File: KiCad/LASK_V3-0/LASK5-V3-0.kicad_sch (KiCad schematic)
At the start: 56 parts, among them IC1 ICM-42688-P, J1 Conn_01x04, J2 JST_02, J3 Conn_01x04_Pin, J4 USB_C_Receptacle, J5 Conn_01x02, J6 Conn_01x06_Pin, J9 Conn_01x04, Q1 IRLML2060, Q2 VP0610T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

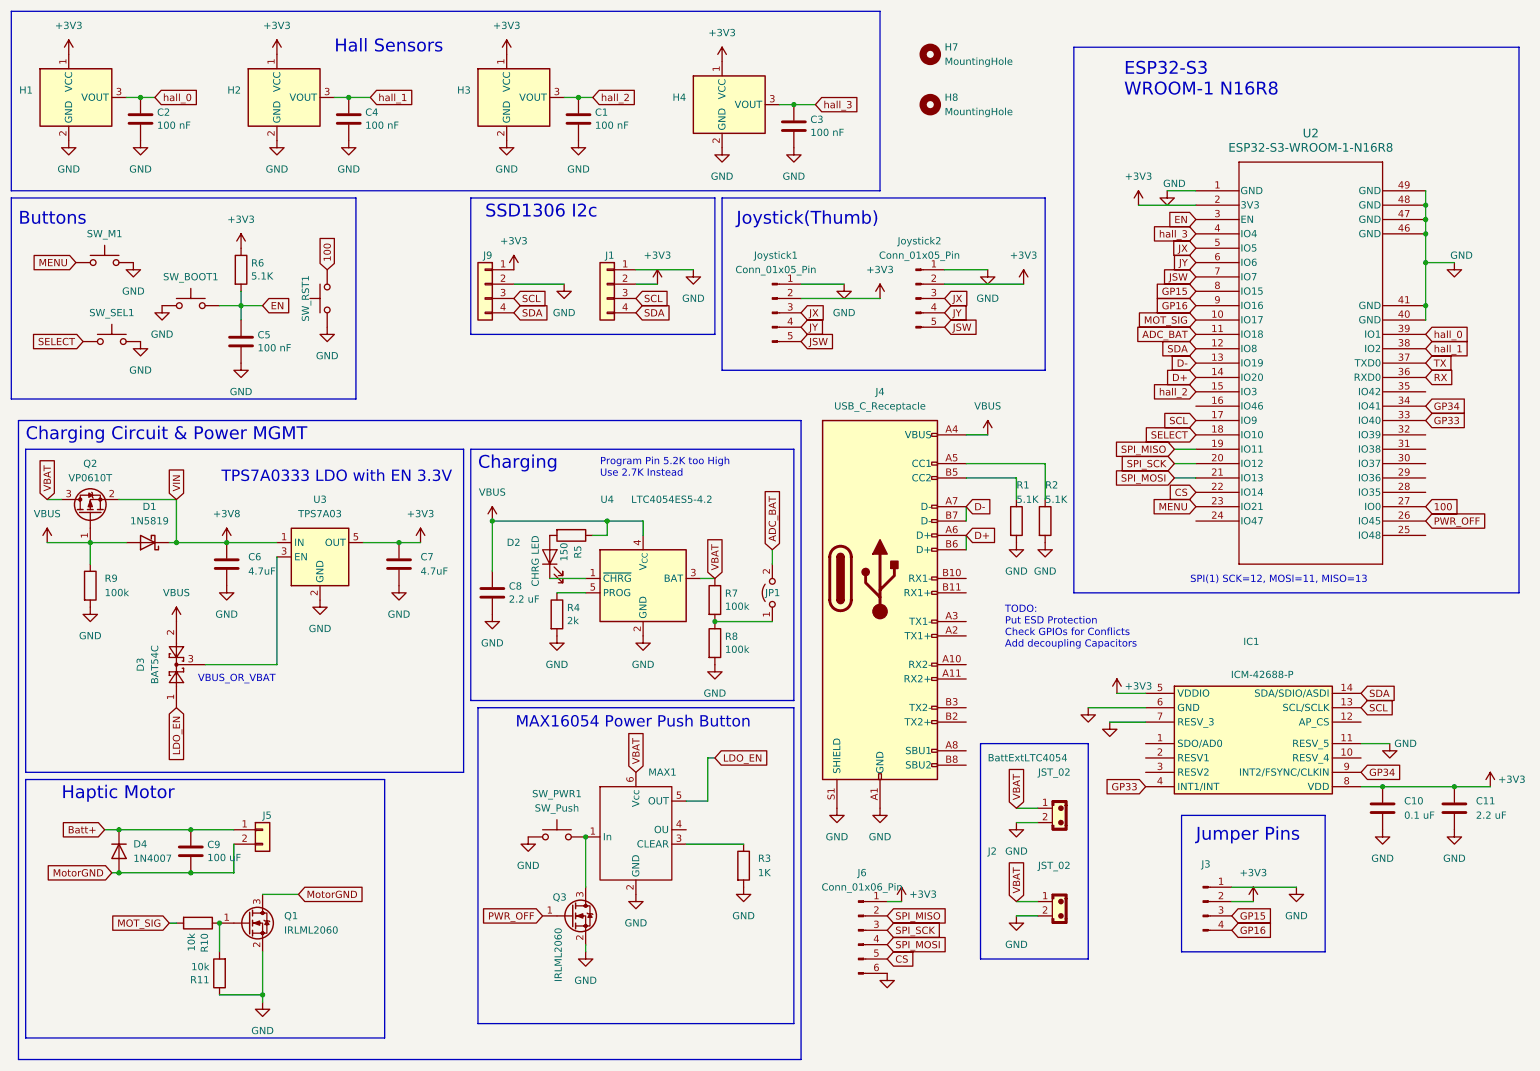
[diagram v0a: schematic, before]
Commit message: Update LASK5 V3 schematic and PCB; add design backups
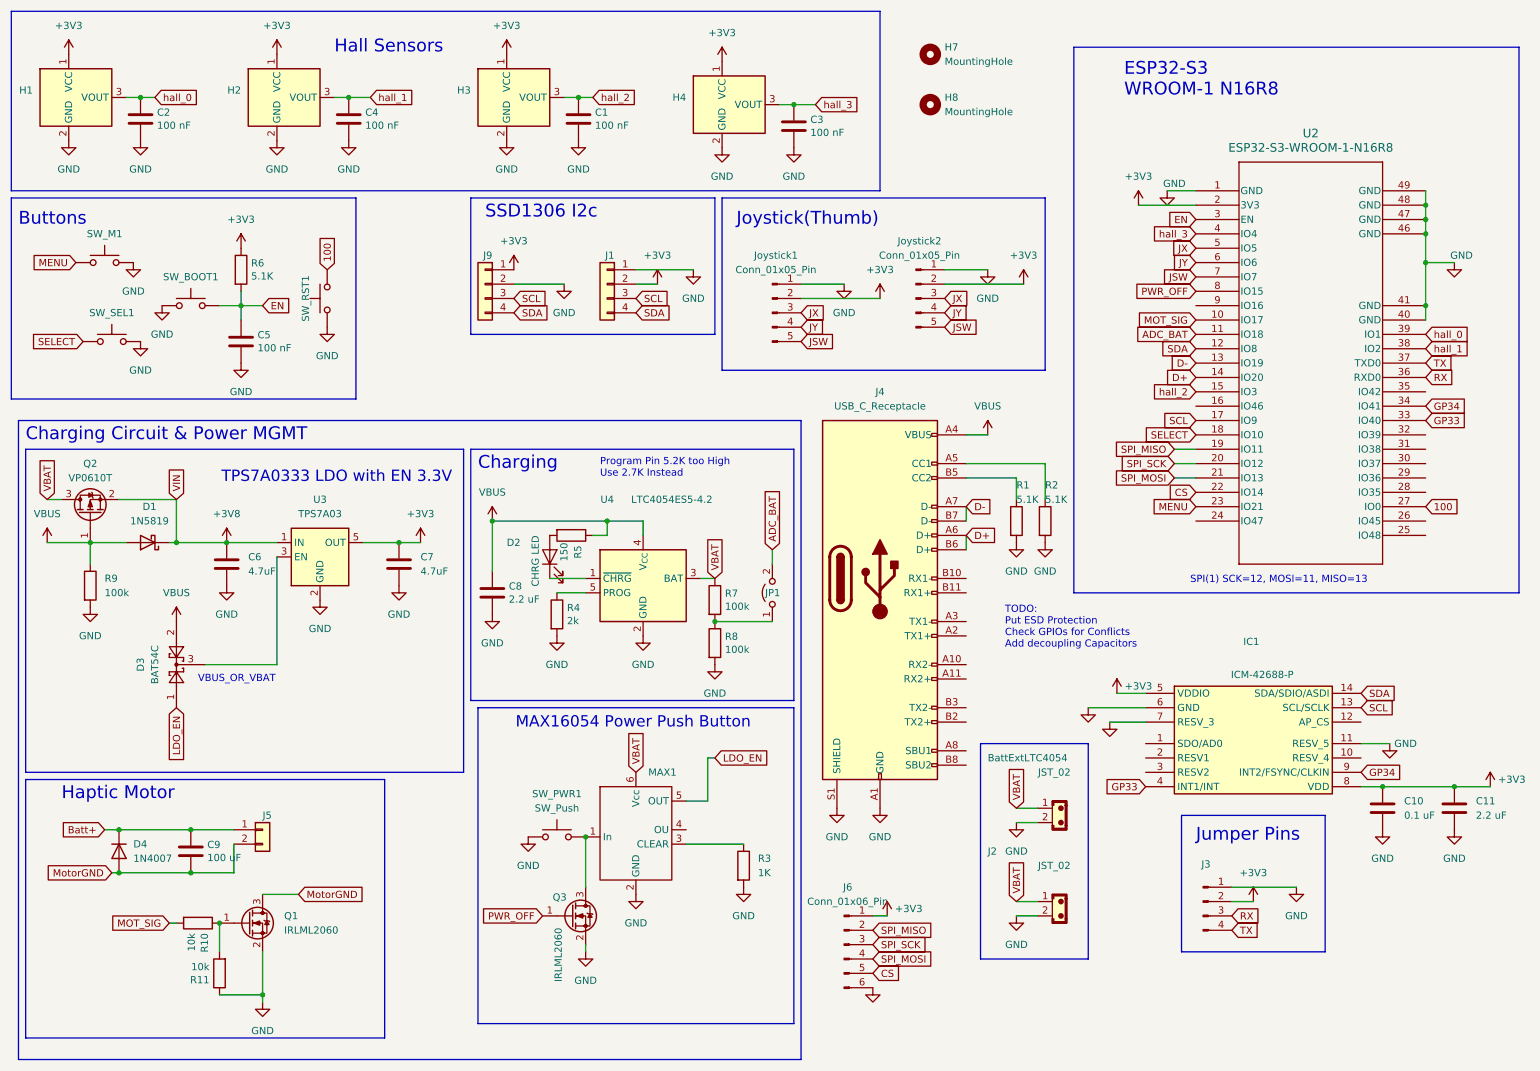
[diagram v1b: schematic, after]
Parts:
- C1, C2, C3, C4, C5: footprint Capacitor_SMD:C_0402_1005Metric -> Capacitor_SMD:C_0603_1608Metric
- MAX1: value ~ -> (none)
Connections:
- net PWR_OFF: now also U2.8 (IO15); no longer U2.26 (IO45)
- net RX: now also J3.3 (Pin_3)
- net TX: now also J3.4 (Pin_4)
- removed net GP15: J3.3 (Pin_3), U2.8 (IO15)
- net GP16: no longer names the net of U2.9 (IO16)
- net GP16: no longer J3.4 (Pin_4)
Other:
- moved on the sheet: J6
